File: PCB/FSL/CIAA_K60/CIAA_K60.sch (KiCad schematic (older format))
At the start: 11 parts

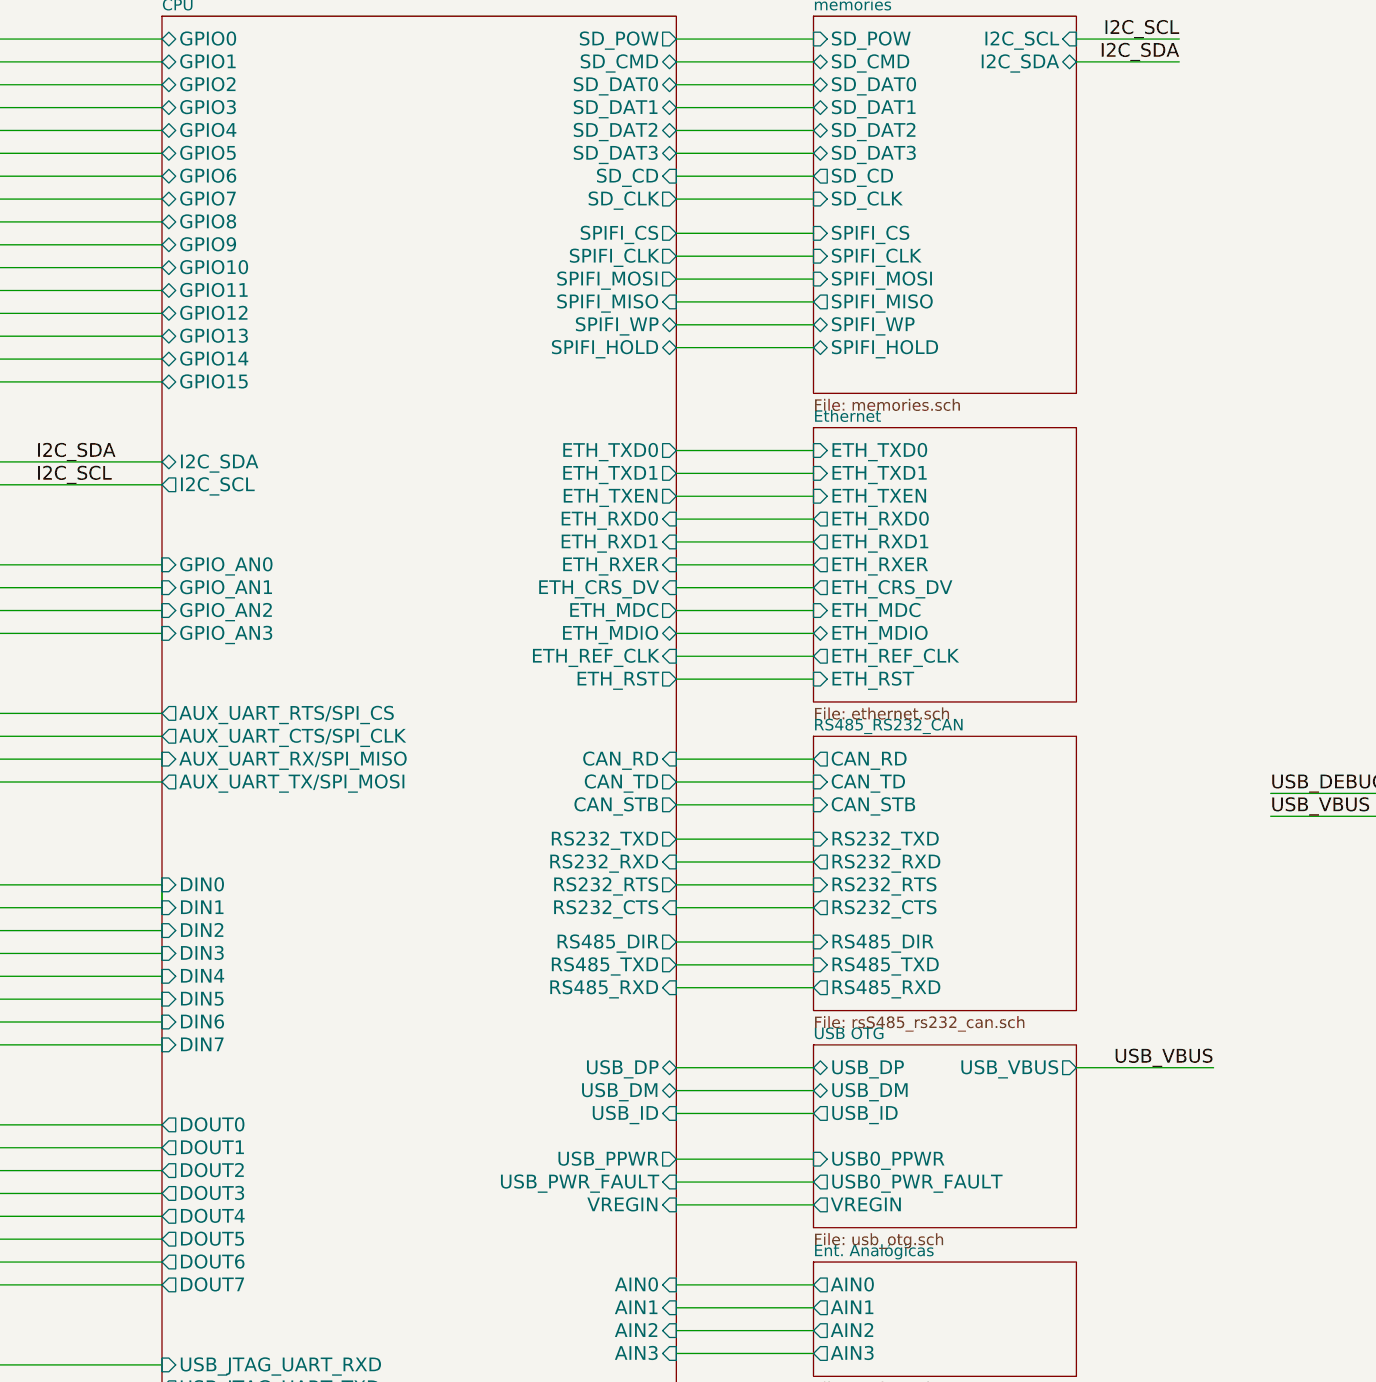
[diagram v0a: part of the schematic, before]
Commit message: Actualizacion de esquematicos. Circuito impreso y modelos 3D
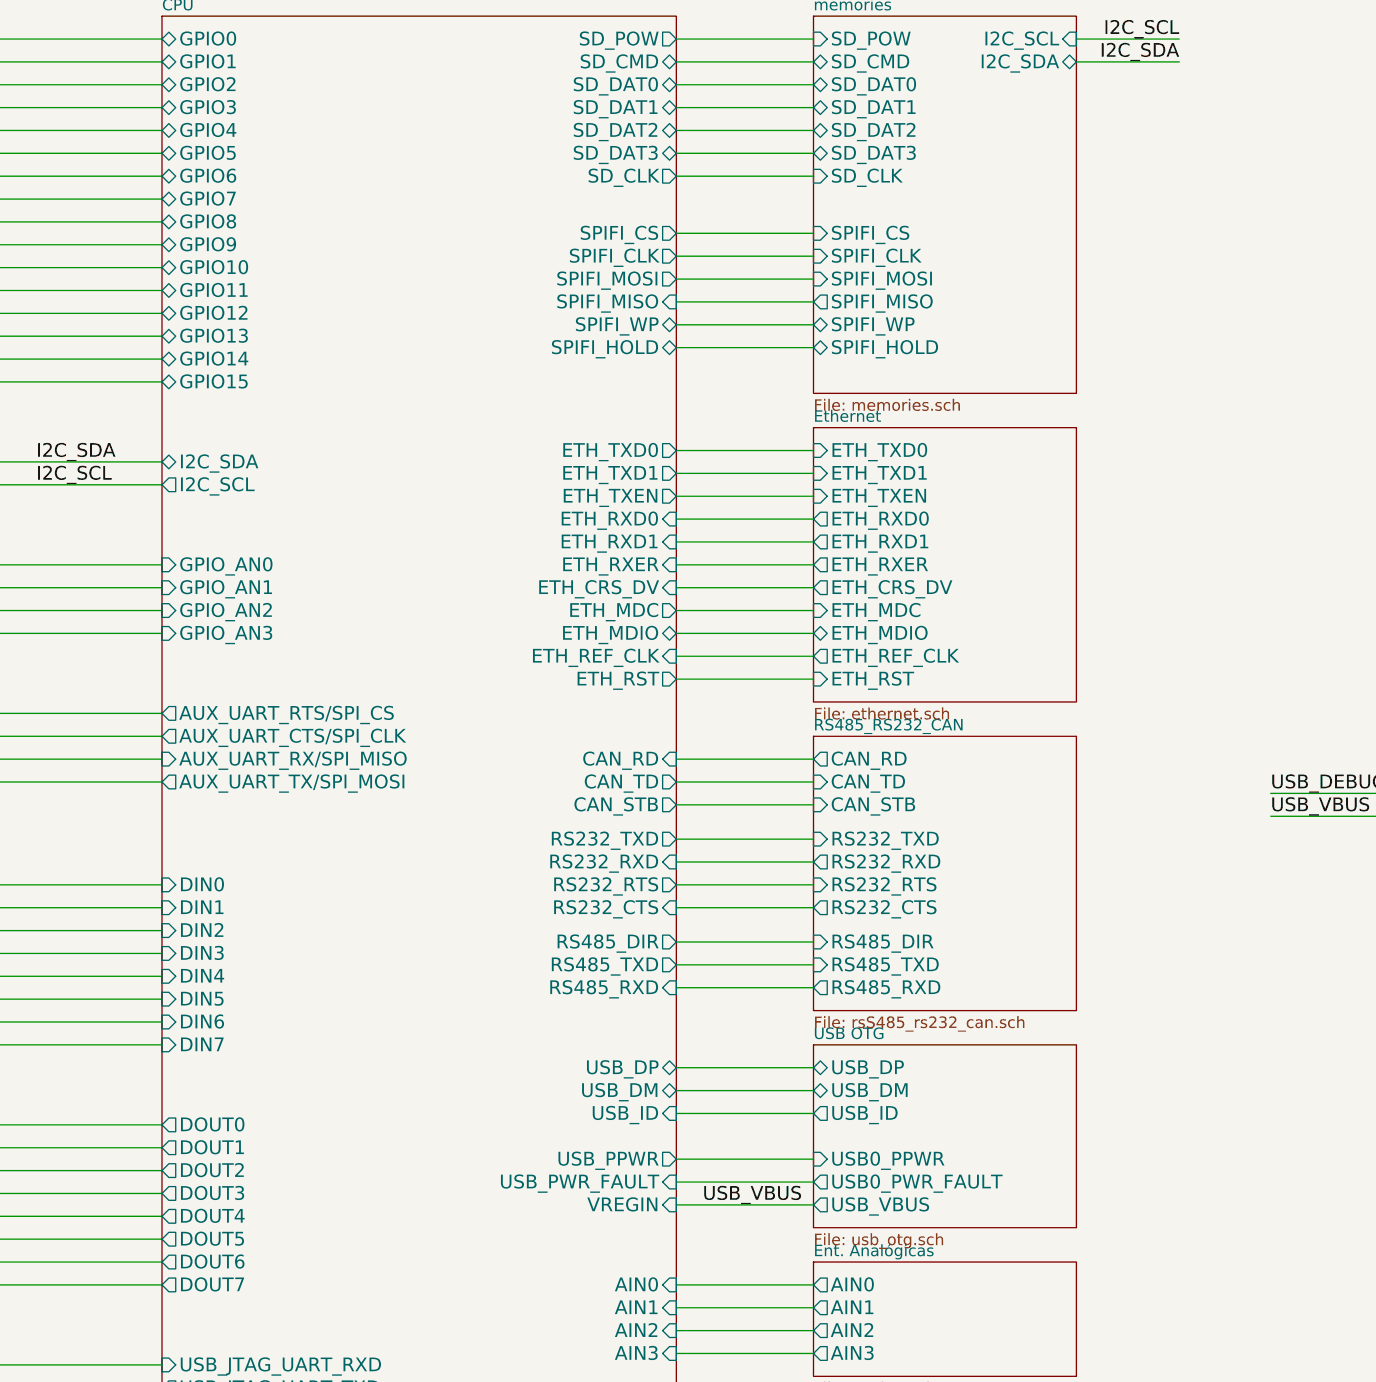
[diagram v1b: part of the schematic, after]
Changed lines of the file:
@@
 Sheet 1 13
 Title "CIAA Freescale - Esquemático jerárquico"
-Date "26 jun 2014"
+Date "15 jul 2014"
 Rev "1.0"
 Comp "CIAA - COMPUTADORA INDUSTRIAL ABIERTA ARGENTINA. Versión FSL (Freescale K60)"
@@
 F8 "SD_DAT2" B R 5200 1350 60
 F9 "SD_DAT3" B R 5200 1450 60
-F10 "SD_CD" I R 5200 1550 60
-F11 "GPIO2" B L 2950 1150 60
-F12 "GPIO3" B L 2950 1250 60
-F13 "GPIO4" B L 2950 1350 60
-F14 "GPIO5" B L 2950 1450 60
-F15 "CAN_RD" I R 5200 4100 60
-F16 "CAN_TD" O R 5200 4200 60
-F17 "RS232_TXD" O R 5200 4450 60
-F18 "RS232_RXD" I R 5200 4550 60
-F19 "DOUT7" O L 2950 6400 60
-F20 "DIN0" I L 2950 4650 60
-F21 "DIN1" I L 2950 4750 60
-F22 "DIN2" I L 2950 4850 60
-F23 "DIN3" I L 2950 4950 60
-F24 "DOUT0" O L 2950 5700 60
-F25 "DOUT1" O L 2950 5800 60
-F26 "DOUT2" O L 2950 5900 60
-F27 "DOUT3" O L 2950 6000 60
-F28 "DOUT4" O L 2950 6100 60
-F29 "DOUT5" O L 2950 6200 60
-F30 "DOUT6" O L 2950 6300 60
-F31 "GPIO6" B L 2950 1550 60
-F32 "GPIO7" B L 2950 1650 60
-F33 "RS485_DIR" O R 5200 4900 60
-F34 "GPIO8" B L 2950 1750 60
-F35 "GPIO9" B L 2950 1850 60
-F36 "GPIO10" B L 2950 1950 60
-F37 "GPIO11" B L 2950 2050 60
-F38 "USB_DP" B R 5200 5450 60
-F39 "USB_DM" B R 5200 5550 60
-F40 "USB_ID" I R 5200 5650 60
-F41 "RS485_TXD" O R 5200 5000 60
-F42 "RS485_RXD" I R 5200 5100 60
-F43 "AIN0" I R 5200 6400 60
-F44 "DIN4" I L 2950 5050 60
-F45 "AIN1" I R 5200 6500 60
-F46 "AIN2" I R 5200 6600 60
-F47 "AIN3" I R 5200 6700 60
-F48 "DIN7" I L 2950 5350 60
-F49 "DIN6" I L 2950 5250 60
-F50 "DIN5" I L 2950 5150 60
-F51 "ETH_TXD0" O R 5200 2750 60
-F52 "ETH_TXD1" O R 5200 2850 60
-F53 "ETH_RXD0" I R 5200 3050 60
-F54 "ETH_RXD1" I R 5200 3150 60
-F55 "ETH_RXER" I R 5200 3250 60
-F56 "ETH_CRS_DV" I R 5200 3350 60
-F57 "ETH_MDC" O R 5200 3450 60
-F58 "ETH_RST" O R 5200 3750 60
-F59 "ETH_TXEN" O R 5200 2950 60
-F60 "ETH_REF_CLK" I R 5200 3650 60
-F61 "RS232_CTS" I R 5200 4750 60
-F62 "RS232_RTS" O R 5200 4650 60
-F63 "CAN_STB" O R 5200 4300 60
-F64 "GPIO12" B L 2950 2150 60
-F65 "GPIO13" B L 2950 2250 60
-F66 "GPIO14" B L 2950 2350 60
-F67 "GPIO_AN1" I L 2950 3350 60
-F68 "GPIO_AN2" I L 2950 3450 60
-F69 "GPIO_AN3" I L 2950 3550 60
-F70 "USB_PWR_FAULT" I R 5200 5950 60
-F71 "USB_PPWR" O R 5200 5850 60
-F72 "AUX_UART_RX/SPI_MISO" I L 2950 4100 60
-F73 "AUX_UART_TX/SPI_MOSI" O L 2950 4200 60
-F74 "I2C_SCL" O L 2950 2900 60
-F75 "I2C_SDA" B L 2950 2800 60
-F76 "SPIFI_MOSI" O R 5200 2000 60
-F77 "SPIFI_MISO" I R 5200 2100 60
-F78 "SPIFI_CS" O R 5200 1800 60
-F79 "SPIFI_HOLD" B R 5200 2300 60
-F80 "SPIFI_WP" B R 5200 2200 60
-F81 "SPIFI_CLK" O R 5200 1900 60
-F82 "USB_JTAG_UART_TXD" O L 2950 6850 60
-F83 "USB_JTAG_UART_RXD" I L 2950 6750 60
-F84 "TCK" I L 2950 7300 60
-F85 "TDI" I L 2950 7500 60
-F86 "TDO" O L 2950 7400 60
-F87 "TMS" I L 2950 7200 60
-F88 "VREGIN" I R 5200 6050 60
-F89 "VBAT" I R 5200 7450 60
-F90 "GPIO15" B L 2950 2450 60
-F91 "GPIO_AN0" I L 2950 3250 60
-F92 "AUX_UART_RTS/SPI_CS" O L 2950 3900 60
-F93 "AUX_UART_CTS/SPI_CLK" O L 2950 4000 60
-F94 "SD_CLK" O R 5200 1650 60
-F95 "ETH_MDIO" B R 5200 3550 60
-F96 "DAC_OUT" O R 5200 7200 60
-F97 "RESET" I L 2950 6950 60
+F10 "GPIO2" B L 2950 1150 60
+F11 "GPIO3" B L 2950 1250 60
+F12 "GPIO4" B L 2950 1350 60
+F13 "GPIO5" B L 2950 1450 60
+F14 "CAN_RD" I R 5200 4100 60
+F15 "CAN_TD" O R 5200 4200 60
+F16 "RS232_TXD" O R 5200 4450 60
+F17 "RS232_RXD" I R 5200 4550 60
+F18 "DOUT7" O L 2950 6400 60
+F19 "DIN0" I L 2950 4650 60
+F20 "DIN1" I L 2950 4750 60
+F21 "DIN2" I L 2950 4850 60
+F22 "DIN3" I L 2950 4950 60
+F23 "DOUT0" O L 2950 5700 60
+F24 "DOUT1" O L 2950 5800 60
+F25 "DOUT2" O L 2950 5900 60
+F26 "DOUT3" O L 2950 6000 60
+F27 "DOUT4" O L 2950 6100 60
+F28 "DOUT5" O L 2950 6200 60
+F29 "DOUT6" O L 2950 6300 60
+F30 "GPIO6" B L 2950 1550 60
+F31 "GPIO7" B L 2950 1650 60
+F32 "RS485_DIR" O R 5200 4900 60
+F33 "GPIO8" B L 2950 1750 60
+F34 "GPIO9" B L 2950 1850 60
+F35 "GPIO10" B L 2950 1950 60
+F36 "GPIO11" B L 2950 2050 60
+F37 "USB_DP" B R 5200 5450 60
+F38 "USB_DM" B R 5200 5550 60
+F39 "USB_ID" I R 5200 5650 60
+F40 "RS485_TXD" O R 5200 5000 60
+F41 "RS485_RXD" I R 5200 5100 60
+F42 "AIN0" I R 5200 6400 60
+F43 "DIN4" I L 2950 5050 60
+F44 "AIN1" I R 5200 6500 60
+F45 "AIN2" I R 5200 6600 60
+F46 "AIN3" I R 5200 6700 60
+F47 "DIN7" I L 2950 5350 60
+F48 "DIN6" I L 2950 5250 60
+F49 "DIN5" I L 2950 5150 60
+F50 "ETH_TXD0" O R 5200 2750 60
+F51 "ETH_TXD1" O R 5200 2850 60
+F52 "ETH_RXD0" I R 5200 3050 60
+F53 "ETH_RXD1" I R 5200 3150 60
+F54 "ETH_RXER" I R 5200 3250 60
+F55 "ETH_CRS_DV" I R 5200 3350 60
+F56 "ETH_MDC" O R 5200 3450 60
+F57 "ETH_RST" O R 5200 3750 60
+F58 "ETH_TXEN" O R 5200 2950 60
+F59 "ETH_REF_CLK" I R 5200 3650 60
+F60 "RS232_CTS" I R 5200 4750 60
+F61 "RS232_RTS" O R 5200 4650 60
+F62 "CAN_STB" O R 5200 4300 60
+F63 "GPIO12" B L 2950 2150 60
+F64 "GPIO13" B L 2950 2250 60
+F65 "GPIO14" B L 2950 2350 60
+F66 "GPIO_AN1" I L 2950 3350 60
+F67 "GPIO_AN2" I L 2950 3450 60
+F68 "GPIO_AN3" I L 2950 3550 60
+F69 "USB_PWR_FAULT" I R 5200 5950 60
+F70 "USB_PPWR" O R 5200 5850 60
+F71 "AUX_UART_RX/SPI_MISO" I L 2950 4100 60
+F72 "AUX_UART_TX/SPI_MOSI" O L 2950 4200 60
+F73 "I2C_SCL" O L 2950 2900 60
+F74 "I2C_SDA" B L 2950 2800 60
+F75 "SPIFI_MOSI" O R 5200 2000 60
+F76 "SPIFI_MISO" I R 5200 2100 60
+F77 "SPIFI_CS" O R 5200 1800 60
+F78 "SPIFI_HOLD" B R 5200 2300 60
+F79 "SPIFI_WP" B R 5200 2200 60
+F80 "SPIFI_CLK" O R 5200 1900 60
+F81 "USB_JTAG_UART_TXD" O L 2950 6850 60
+F82 "USB_JTAG_UART_RXD" I L 2950 6750 60
+F83 "TCK" I L 2950 7300 60
+F84 "TDI" I L 2950 7500 60
+F85 "TDO" O L 2950 7400 60
+F86 "TMS" I L 2950 7200 60
+F87 "VREGIN" I R 5200 6050 60
+F88 "VBAT" I R 5200 7450 60
+F89 "GPIO15" B L 2950 2450 60
+F90 "GPIO_AN0" I L 2950 3250 60
+F91 "AUX_UART_RTS/SPI_CS" O L 2950 3900 60
+F92 "AUX_UART_CTS/SPI_CLK" O L 2950 4000 60
+F93 "SD_CLK" O R 5200 1550 60
+F94 "ETH_MDIO" B R 5200 3550 60
+F95 "DAC_OUT" O R 5200 7200 60
+F96 "RESET" I L 2950 6950 60
 $EndSheet
 $Sheet
@@
 F0 "USB OTG" 50
 F1 "usb_otg.sch" 50
-F2 "USB_VBUS" O R 6950 5450 60
+F2 "USB_VBUS" O L 5800 6050 60
 F3 "USB_DM" B L 5800 5550 60
 F4 "USB_DP" B L 5800 5450 60
@@
 F6 "USB0_PPWR" I L 5800 5850 60
 F7 "USB0_PWR_FAULT" O L 5800 5950 60
-F8 "VREGIN" O L 5800 6050 60
 $EndSheet
 $Sheet
@@
 F0 "memories" 50
 F1 "memories.sch" 50
-F2 "SD_CLK" I L 5800 1650 60
+F2 "SD_CLK" I L 5800 1550 60
 F3 "SD_POW" I L 5800 950 60
 F4 "SPIFI_CS" I L 5800 1800 60
@@
 F10 "SPIFI_MOSI" I L 5800 2000 60
 F11 "SPIFI_MISO" O L 5800 2100 60
-F12 "SD_CD" O L 5800 1550 60
-F13 "SD_CMD" B L 5800 1050 60
-F14 "SD_DAT0" B L 5800 1150 60
-F15 "SD_DAT1" B L 5800 1250 60
-F16 "SD_DAT2" B L 5800 1350 60
-F17 "SD_DAT3" B L 5800 1450 60
+F12 "SD_CMD" B L 5800 1050 60
+F13 "SD_DAT0" B L 5800 1150 60
+F14 "SD_DAT1" B L 5800 1250 60
+F15 "SD_DAT2" B L 5800 1350 60
+F16 "SD_DAT3" B L 5800 1450 60
 $EndSheet
 $Sheet
@@
 Text Label 7800 4350 0    60   ~ 0
 USB_VBUS
-Text Label 7550 5450 2    60   ~ 0
-USB_VBUS
 Text Label 2400 6950 0    60   ~ 0
 RESET
@@
 	2150 4650 2950 4650
 Wire Wire Line
-	2950 4650 2950 4750
-Wire Wire Line
 	2950 4750 2150 4750
 Wire Wire Line
@@
 	5200 1450 5800 1450
 Wire Wire Line
-	5800 1550 5200 1550
-Wire Wire Line
-	5200 1650 5800 1650
-Wire Wire Line
 	5800 1800 5200 1800
 Wire Wire Line
@@
 Wire Wire Line
 	5200 7200 5800 7200
-Wire Wire Line
-	7550 5450 6950 5450
 Wire Wire Line
 	5800 5650 5200 5650
@@
 Wire Wire Line
 	10200 5200 10200 5400
+Wire Wire Line
+	5200 1550 5800 1550
+Text Label 5750 6050 2    60   ~ 0
+USB_VBUS
 $EndSCHEMATC

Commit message: Actualizacion de Licencia y avances
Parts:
- added G102: LOGO-CIAA-FSL, LOGO-CIAA, symbol LOGO-CIAA-FSL
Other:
- note removed: "Bajo licencia CERN OHL v.1.2"
- note removed: "Ver: doc/LICENCIA_CIAA_FSL.txt\n"
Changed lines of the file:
@@
 Sheet 1 13
 Title "CIAA Freescale - Esquemático jerárquico"
-Date "15 jul 2014"
+Date "7 aug 2014"
 Rev "1.0"
 Comp "CIAA - COMPUTADORA INDUSTRIAL ABIERTA ARGENTINA. Versión FSL (Freescale K60)"
@@
 	1    0    0    -1
 $EndComp
-Text Notes 8400 6350 0    90   Italic 0
-Bajo licencia CERN OHL v.1.2
-Text Notes 8550 6500 0    70   Italic 0
-Ver: doc/LICENCIA_CIAA_FSL.txt\n
 $Comp
 L OSHWA G101
@@
 Wire Wire Line
 	2150 2900 2950 2900
-Wire Notes Line
-	8350 6050 11150 6050
-Wire Notes Line
-	11150 6050 11150 6750
-Wire Notes Line
-	11150 6750 8350 6750
-Wire Notes Line
-	8350 6750 8350 6050
 Wire Wire Line
 	9900 5300 10350 5300
@@
 Text Label 5750 6050 2    60   ~ 0
 USB_VBUS
+$Comp
+L LOGO-CIAA-FSL G102
+U 1 1 53E304AA
+P 10000 6400
+F 0 "G102" H 10000 5764 60  0001 C CNN
+F 1 "LOGO-CIAA-FSL" H 10000 7036 60  0001 C CNN
+F 2 "LOGO-CIAA" H 10000 6400 60  0001 C CNN
+F 3 "~" H 10000 6400 60  0000 C CNN
+	1    10000 6400
+	1    0    0    -1
+$EndComp
 $EndSCHEMATC

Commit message: - Actualización del diseño
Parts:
- removed G102: LOGO-CIAA-FSL, LOGO-CIAA, symbol LOGO-CIAA-FSL
- added G102: LOGO_CIAA, LOGO-CIAA, symbol LOGO_CIAA
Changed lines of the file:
@@
 Sheet 1 13
 Title "CIAA Freescale - Esquemático jerárquico"
-Date "7 aug 2014"
+Date "8 aug 2014"
 Rev "1.0"
 Comp "CIAA - COMPUTADORA INDUSTRIAL ABIERTA ARGENTINA. Versión FSL (Freescale K60)"
@@
 USB_VBUS
 $Comp
-L LOGO-CIAA-FSL G102
-U 1 1 53E304AA
+L LOGO_CIAA G102
+U 1 1 53E44CA2
 P 10000 6400
-F 0 "G102" H 10000 5764 60  0001 C CNN
-F 1 "LOGO-CIAA-FSL" H 10000 7036 60  0001 C CNN
+F 0 "G102" H 10000 5827 60  0001 C CNN
+F 1 "LOGO_CIAA" H 10000 6973 60  0001 C CNN
 F 2 "LOGO-CIAA" H 10000 6400 60  0001 C CNN
 F 3 "~" H 10000 6400 60  0000 C CNN

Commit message: - Actualizado PCB - Actualizado documentación - Agregado scripts complementarios de kicad.
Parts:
- G102: Descripcion (none) -> LOGO CIAA
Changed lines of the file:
@@
 Sheet 1 13
 Title "CIAA Freescale - Esquemático jerárquico"
-Date "8 aug 2014"
+Date "25 aug 2014"
 Rev "1.0"
 Comp "CIAA - COMPUTADORA INDUSTRIAL ABIERTA ARGENTINA. Versión FSL (Freescale K60)"
@@
 F 2 "LOGO-CIAA" H 10000 6400 60  0001 C CNN
 F 3 "~" H 10000 6400 60  0000 C CNN
+F 4 "LOGO CIAA" H 10000 6400 60  0001 C CNN "Descripcion"
 	1    10000 6400
 	1    0    0    -1
